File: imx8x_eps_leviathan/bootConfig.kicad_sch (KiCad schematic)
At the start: 24 parts, among them SW1 SW_DIP_x01, U18 BD2204GUL-E2

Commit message: Updated board name
No desc. needed
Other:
- title: Leviathan 1-A -> Leviathan V1
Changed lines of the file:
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@@
 	(paper "A4")
 	(title_block
-		(title "Leviathan 1-A")
+		(title "Leviathan V1")
 		(date "2025-10-29")
-		(rev "1-A")
+		(rev "V1")
 		(company "Bronco Space Lab")
 		(comment 1 "By Luca Lanzillotta & John Pollack")
@@
 	(text "uSD Card Connector"
 		(exclude_from_sim no)
-		(at 103.505 15.24 0)
+		(at 103.632 15.24 0)
 		(effects
 			(font
@@
 	)
 	(junction
-		(at 44.45 42.545)
+		(at 44.45 42.672)
 		(diameter 0)
 		(color 0 0 0 0)
@@
 	)
 	(no_connect
-		(at 44.45 47.625)
+		(at 44.45 47.752)
 	)
 	(no_connect
-		(at 67.31 50.165)
+		(at 67.31 50.292)
 	)
 	(wire
@@
 	(wire
 		(pts
-			(xy 67.31 47.625) (xy 71.12 47.625)
+			(xy 67.31 47.752) (xy 71.12 47.752)
 		)
 		(stroke
@@
 	(wire
 		(pts
-			(xy 41.91 50.165) (xy 44.45 50.165)
+			(xy 41.91 50.292) (xy 44.45 50.292)
 		)
 		(stroke
@@
 	(wire
 		(pts
-			(xy 35.56 42.545) (xy 44.45 42.545)
+			(xy 35.56 42.672) (xy 44.45 42.672)
 		)
 		(stroke
@@
 	(wire
 		(pts
-			(xy 24.13 42.545) (xy 24.13 43.815)
+			(xy 24.13 42.672) (xy 24.13 43.942)
 		)
 		(stroke
@@
 	(wire
 		(pts
-			(xy 67.31 45.085) (xy 71.12 45.085)
+			(xy 67.31 45.212) (xy 71.12 45.212)
 		)
 		(stroke
@@
 	(wire
 		(pts
-			(xy 27.94 42.545) (xy 24.13 42.545)
+			(xy 27.94 42.672) (xy 24.13 42.672)
 		)
 		(stroke
@@
 	(wire
 		(pts
-			(xy 44.45 42.545) (xy 44.45 41.275)
+			(xy 44.45 42.672) (xy 44.45 41.402)
 		)
 		(stroke
@@
 	(wire
 		(pts
-			(xy 44.45 42.545) (xy 44.45 45.085)
+			(xy 44.45 42.672) (xy 44.45 45.212)
 		)
 		(stroke
@@
 	(global_label "X_CONN_USDHC1_RESET_B"
 		(shape input)
-		(at 41.91 50.165 180)
+		(at 41.91 50.292 180)
 		(fields_autoplaced yes)
 		(effects
@@
 		)
 		(property "Intersheetrefs" "${INTERSHEET_REFS}"
-			(at 13.9483 50.165 0)
+			(at 13.9483 50.292 0)
 			(effects
 				(font
@@
 	(global_label "SD1_SPWR"
 		(shape input)
-		(at 71.12 45.085 0)
+		(at 71.12 45.212 0)
 		(fields_autoplaced yes)
 		(effects
@@
 		)
 		(property "Intersheetrefs" "${INTERSHEET_REFS}"
-			(at 83.9627 45.085 0)
+			(at 83.9627 45.212 0)
 			(effects
 				(font
@@
 	(symbol
 		(lib_id "power:GND")
-		(at 24.13 43.815 0)
+		(at 24.13 43.942 0)
 		(unit 1)
 		(exclude_from_sim no)
@@
 		(dnp no)
 		(property "Reference" "#PWR054"
-			(at 24.13 50.165 0)
+			(at 24.13 50.292 0)
 			(effects
 				(font
@@
 		)
 		(property "Value" "GND"
-			(at 24.13 47.625 0)
+			(at 24.13 47.752 0)
 			(effects
 				(font
@@
 		)
 		(property "Footprint" ""
-			(at 24.13 43.815 0)
+			(at 24.13 43.942 0)
 			(effects
 				(font
@@
 		)
 		(property "Datasheet" ""
-			(at 24.13 43.815 0)
+			(at 24.13 43.942 0)
 			(effects
 				(font
@@
 		)
 		(property "Description" "Power symbol creates a global label with name \"GND\" , ground"
-			(at 24.13 43.815 0)
+			(at 24.13 43.942 0)
 			(effects
 				(font
@@
 	(symbol
 		(lib_id "power:GND")
-		(at 71.12 47.625 0)
+		(at 71.12 47.752 0)
 		(unit 1)
 		(exclude_from_sim no)
@@
 		(dnp no)
 		(property "Reference" "#PWR058"
-			(at 71.12 53.975 0)
+			(at 71.12 54.102 0)
 			(effects
 				(font
@@
 		)
 		(property "Value" "GND"
-			(at 71.12 51.435 0)
+			(at 71.12 51.562 0)
 			(effects
 				(font
@@
 		)
 		(property "Footprint" ""
-			(at 71.12 47.625 0)
+			(at 71.12 47.752 0)
 			(effects
 				(font
@@
 		)
 		(property "Datasheet" ""
-			(at 71.12 47.625 0)
+			(at 71.12 47.752 0)
 			(effects
 				(font
@@
 		)
 		(property "Description" "Power symbol creates a global label with name \"GND\" , ground"
-			(at 71.12 47.625 0)
+			(at 71.12 47.752 0)
 			(effects
 				(font
@@
 	(symbol
 		(lib_id "imx8_carrier_board_symbol_library:BD2204GUL-E2")
-		(at 55.88 47.625 0)
+		(at 55.88 47.752 0)
 		(unit 1)
 		(exclude_from_sim no)
@@
 		(dnp no)
 		(property "Reference" "U18"
-			(at 55.626 47.117 0)
+			(at 55.626 47.244 0)
 			(effects
 				(font
@@
 		)
 		(property "Value" "BD2204GUL-E2"
-			(at 55.88 53.975 0)
+			(at 55.88 54.102 0)
 			(effects
 				(font
@@
 		)
 		(property "Footprint" "imx8_carrier_board_footprints:BGA-6_L1.5-W1.0-P0.50_BD2204GUL-E2"
-			(at 55.88 57.785 0)
+			(at 55.88 57.912 0)
 			(effects
 				(font
@@
 		)
 		(property "Datasheet" "https://lcsc.com/product-detail/Power-Distribution-Switches_ROHM-Semicon-BD2204GUL-E2_C314699.html?s_z=n_BD2204GUL-E2"
-			(at 55.88 47.625 0)
+			(at 55.88 47.752 0)
 			(effects
 				(font
@@
 		)
 		(property "Description" ""
-			(at 55.88 47.625 0)
+			(at 55.88 47.752 0)
 			(effects
 				(font
@@
 		)
 		(property "LCSC Part" "C314699"
-			(at 55.88 60.325 0)
+			(at 55.88 60.452 0)
 			(effects
 				(font
@@
 	(symbol
 		(lib_id "Device:C")
-		(at 31.75 42.545 90)
+		(at 31.75 42.672 90)
 		(mirror x)
 		(unit 1)
@@
 		(dnp no)
 		(property "Reference" "C58"
-			(at 33.782 39.243 90)
+			(at 33.782 39.37 90)
 			(effects
 				(font
@@
 		)
 		(property "Value" "100nF"
-			(at 35.052 45.847 90)
+			(at 35.052 45.974 90)
 			(effects
 				(font
@@
 		)
 		(property "Footprint" "EPS:C0402"
-			(at 35.56 43.5102 0)
+			(at 35.56 43.6372 0)
 			(effects
 				(font
@@
 		)
 		(property "Datasheet" "~"
-			(at 31.75 42.545 0)
+			(at 31.75 42.672 0)
 			(effects
 				(font
@@
 		)
 		(property "Description" "Unpolarized capacitor"
-			(at 31.75 47.879 90)
+			(at 31.75 48.006 90)
 			(effects
 				(font
@@
 	(symbol
 		(lib_id "power:+3.3V")
-		(at 44.45 41.275 0)
+		(at 44.45 41.402 0)
 		(unit 1)
 		(exclude_from_sim no)
@@
 		(dnp no)
 		(property "Reference" "#PWR057"
-			(at 44.45 45.085 0)
+			(at 44.45 45.212 0)
 			(effects
 				(font
@@
 		)
 		(property "Value" "+3.3V_OBC_Perif"
-			(at 49.784 37.719 0)
+			(at 49.784 37.846 0)
 			(effects
 				(font
@@
 		)
 		(property "Footprint" ""
-			(at 44.45 41.275 0)
+			(at 44.45 41.402 0)
 			(effects
 				(font
@@
 		)
 		(property "Datasheet" ""
-			(at 44.45 41.275 0)
+			(at 44.45 41.402 0)
 			(effects
 				(font
@@
 		)
 		(property "Description" "Power symbol creates a global label with name \"+3.3V\""
-			(at 44.45 41.275 0)
+			(at 44.45 41.402 0)
 			(effects
 				(font

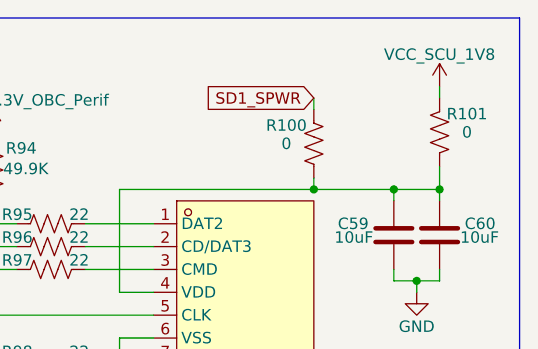
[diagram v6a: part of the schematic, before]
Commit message: Working on Simulation Models
Got the TPS1 working. Got the LT8612 working. Working on the Comparator network for the watchdog
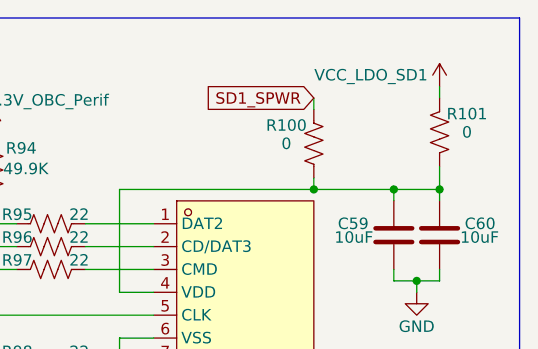
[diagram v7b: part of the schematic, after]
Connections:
- net VCC_LDO_SD1: now also R101.2
- net VCC_SCU_1V8: no longer R101.2
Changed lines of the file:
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@@
-	)
-	(symbol
-		(lib_id "power:Vdrive")
-		(at 200.66 20.32 0)
-		(unit 1)
-		(exclude_from_sim no)
-		(in_bom yes)
-		(on_board yes)
-		(dnp no)
-		(property "Reference" "#PWR063"
-			(at 200.66 24.13 0)
-			(effects
-				(font
-					(size 1.27 1.27)
-				)
-				(hide yes)
-			)
-		)
-		(property "Value" "VCC_SCU_1V8"
-			(at 200.66 16.764 0)
-			(effects
-				(font
-					(size 1.27 1.27)
-				)
-			)
-		)
-		(property "Footprint" ""
-			(at 200.66 20.32 0)
-			(effects
-				(font
-					(size 1.27 1.27)
-				)
-				(hide yes)
-			)
-		)
-		(property "Datasheet" ""
-			(at 200.66 20.32 0)
-			(effects
-				(font
-					(size 1.27 1.27)
-				)
-				(hide yes)
-			)
-		)
-		(property "Description" "Power symbol creates a global label with name \"Vdrive\""
-			(at 200.66 20.32 0)
-			(effects
-				(font
-					(size 1.27 1.27)
-				)
-				(hide yes)
-			)
-		)
-		(pin "1"
-		)
-		(instances
-			(project "imx8x_eps_leviathan"
-				(path "/bd3af9f3-19df-4a2f-8b54-98c48cea082e/1b5b2e76-614d-4307-9232-e06f7c77302d/523ae3db-78a2-4812-be5f-87bab42ef950"
-					(reference "#PWR063")
-					(unit 1)
-				)
-			)
-		)
 	)
 	(symbol
@@
 					(unit 1)
 				)
+			)
+		)
+	)
+	(symbol
+		(lib_id "imx8_carrier_board_symbol_library:VCC_LDO_SD1")
+		(at 200.66 20.32 0)
+		(unit 1)
+		(exclude_from_sim no)
+		(in_bom yes)
+		(on_board yes)
+		(dnp no)
+		(property "Reference" "#PWR063"
+			(at 200.66 24.13 0)
+			(effects
+				(font
+					(size 1.27 1.27)
+				)
+				(hide yes)
+			)
+		)
+		(property "Value" "VCC_LDO_SD1"
+			(at 193.04 19.05 0)
+			(effects
+				(font
+					(size 1.27 1.27)
+				)
+			)
+		)
+		(property "Footprint" ""
+			(at 200.66 20.32 0)
+			(effects
+				(font
+					(size 1.27 1.27)
+				)
+				(hide yes)
+			)
+		)
+		(property "Datasheet" ""
+			(at 200.66 20.32 0)
+			(effects
+				(font
+					(size 1.27 1.27)
+				)
+				(hide yes)
+			)
+		)
+		(property "Description" "Power symbol creates a global label with name \"VCC\""
+			(at 200.66 20.32 0)
+			(effects
+				(font
+					(size 1.27 1.27)
+				)
+				(hide yes)
+			)
+		)
+		(pin "1"
+		)
+		(instances
+			(project "imx8x_eps_leviathan"
+				(path "/bd3af9f3-19df-4a2f-8b54-98c48cea082e/1b5b2e76-614d-4307-9232-e06f7c77302d/523ae3db-78a2-4812-be5f-87bab42ef950"
+					(reference "#PWR063")
+					(unit 1)
+				)

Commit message: Added Phytecs last recommended changes
Updated 3/17/26
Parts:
- removed R101: 0, EPS:R0402, symbol Device:R_US
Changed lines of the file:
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@@
-	)
-	(junction
-		(at 200.66 31.75)
-		(diameter 0)
-		(color 0 0 0 0)
 	)
 	(junction
@@
 	(wire
 		(pts
-			(xy 200.66 20.32) (xy 200.66 21.59)
-		)
-		(stroke
-			(width 0)
-			(type default)
-		)
-	)
-	(wire
-		(pts
 			(xy 147.32 33.02) (xy 147.32 53.34)
 		)
@@
 		(pts
 			(xy 124.46 33.02) (xy 124.46 38.1)
-		)
-		(stroke
-			(width 0)
-			(type default)
-		)
-	)
-	(wire
-		(pts
-			(xy 200.66 29.21) (xy 200.66 31.75)
 		)
 		(stroke
@@
 				(path "/bd3af9f3-19df-4a2f-8b54-98c48cea082e/1b5b2e76-614d-4307-9232-e06f7c77302d/523ae3db-78a2-4812-be5f-87bab42ef950"
 					(reference "#PWR056")
-					(unit 1)
-				)
-			)
-		)
-	)
-	(symbol
-		(lib_id "imx8_carrier_board_symbol_library:VCC_LDO_SD1")
-		(at 200.66 20.32 0)
-		(unit 1)
-		(exclude_from_sim no)
-		(in_bom yes)
-		(on_board yes)
-		(dnp no)
-		(property "Reference" "#PWR063"
-			(at 200.66 24.13 0)
-			(effects
-				(font
-					(size 1.27 1.27)
-				)
-				(hide yes)
-			)
-		)
-		(property "Value" "VCC_LDO_SD1"
-			(at 193.04 19.05 0)
-			(effects
-				(font
-					(size 1.27 1.27)
-				)
-			)
-		)
-		(property "Footprint" ""
-			(at 200.66 20.32 0)
-			(effects
-				(font
-					(size 1.27 1.27)
-				)
-				(hide yes)
-			)
-		)
-		(property "Datasheet" ""
-			(at 200.66 20.32 0)
-			(effects
-				(font
-					(size 1.27 1.27)
-				)
-				(hide yes)
-			)
-		)
-		(property "Description" "Power symbol creates a global label with name \"VCC\""
-			(at 200.66 20.32 0)
-			(effects
-				(font
-					(size 1.27 1.27)
-				)
-				(hide yes)
-			)
-		)
-		(pin "1"
-		)
-		(instances
-			(project "imx8x_eps_leviathan"
-				(path "/bd3af9f3-19df-4a2f-8b54-98c48cea082e/1b5b2e76-614d-4307-9232-e06f7c77302d/523ae3db-78a2-4812-be5f-87bab42ef950"
-					(reference "#PWR063")
 					(unit 1)
 				)
@@
 					(unit 1)
 				)
-			)
-		)
-	)
-	(symbol
-		(lib_id "Device:R_US")
-		(at 200.66 25.4 0)
-		(mirror x)
-		(unit 1)
-		(exclude_from_sim no)
-		(in_bom yes)
-		(on_board yes)
-		(dnp no)
-		(property "Reference" "R101"
-			(at 203.708 23.368 0)
-			(effects
-				(font
-					(size 1.27 1.27)
-				)
-			)
-		)
-		(property "Value" "0"
-			(at 203.708 25.4 0)
-			(effects
-				(font
-					(size 1.27 1.27)
-				)
-			)
-		)
-		(property "Footprint" "EPS:R0402"
-			(at 201.676 25.146 90)
-			(effects
-				(font
-					(size 1.27 1.27)
-				)
-				(hide yes)
-			)
-		)
-		(property "Datasheet" "~"
-			(at 200.66 25.4 0)
-			(effects
-				(font
-					(size 1.27 1.27)
-				)
-				(hide yes)
-			)
-		)
-		(property "Description" "Resistor, US symbol"
-			(at 200.66 25.4 0)
-			(effects
-				(font
-					(size 1.27 1.27)
-				)
-				(hide yes)
-			)
-		)
-		(pin "1"
-		)
-		(pin "2"
-		)
-		(instances
-			(project "imx8x_eps_leviathan"
-				(path "/bd3af9f3-19df-4a2f-8b54-98c48cea082e/1b5b2e76-614d-4307-9232-e06f7c77302d/523ae3db-78a2-4812-be5f-87bab42ef950"
-					(reference "R101")
-					(unit 1)
-				)
